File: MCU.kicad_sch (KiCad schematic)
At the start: 35 parts, among them IC9 ATSAMD21G18A-MF, J10 SAMTEC_SSW-106-01-L-S, J7 SAMTEC_SSW-108-01-G-S, J8 SAMTEC_SSW-110-01-G-S, J9 SAMTEC_SSW-108-01-G-S, Q1 XTAL_32.768KHZ_ABRACON_ABS09-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

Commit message: Added new ADC
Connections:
- net MCU_SCL: no longer IC9.32 (PA23), J8.10
- net MCU_SDA: no longer IC9.31 (PA22), J8.9
- net MCU_RxD renamed MCU_RX
- net MCU_TxD renamed MCU_TX
- new net P.A22: IC9.31 (PA22), J8.9
- new net P.A23: IC9.32 (PA23), J8.10
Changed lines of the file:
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@@
 		)
 	)
-	(text_box "Routing note:\n- Placement of female headers must match Arduino Zero Hat"
+	(text_box "Routing note:\n- Placement of female headers must match Arduino Zero Shield"
 		(exclude_from_sim no)
 		(at 285.75 43.18 0)
@@
 		)
 	)
-	(label "MCU_RxD"
+	(label "MCU_RX"
 		(at 201.93 68.58 180)
 		(fields_autoplaced yes)
@@
 		)
 	)
-	(label "MCU_TxD"
+	(label "MCU_TX"
 		(at 350.52 36.83 0)
 		(fields_autoplaced yes)
@@
 		)
 	)
-	(label "P.A22"
+	(label "MCU_SDA"
 		(at 350.52 29.21 0)
 		(fields_autoplaced yes)
@@
 		)
 	)
-	(label "MCU_RxD"
+	(label "MCU_RX"
 		(at 350.52 40.64 0)
 		(fields_autoplaced yes)
@@
 		)
 	)
-	(label "P.A23"
+	(label "MCU_SCL"
 		(at 350.52 33.02 0)
 		(fields_autoplaced yes)
@@
 		)
 	)
-	(label "MCU_TxD"
+	(label "MCU_TX"
 		(at 201.93 66.04 180)
 		(fields_autoplaced yes)
@@
 		)
 	)
-	(label "P.A22"
+	(label "MCU_SDA"
 		(at 107.95 111.76 180)
 		(fields_autoplaced yes)
@@
 		)
 	)
-	(label "P.A23"
+	(label "MCU_SCL"
 		(at 107.95 114.3 180)
 		(fields_autoplaced yes)
@@
 		)
 	)
-	(hierarchical_label "MCU_TxD"
+	(hierarchical_label "MCU_TX"
 		(shape output)
 		(at 374.65 36.83 0)
@@
 		)
 	)
-	(hierarchical_label "MCU_RxD"
+	(hierarchical_label "MCU_RX"
 		(shape input)
 		(at 374.65 40.64 0)

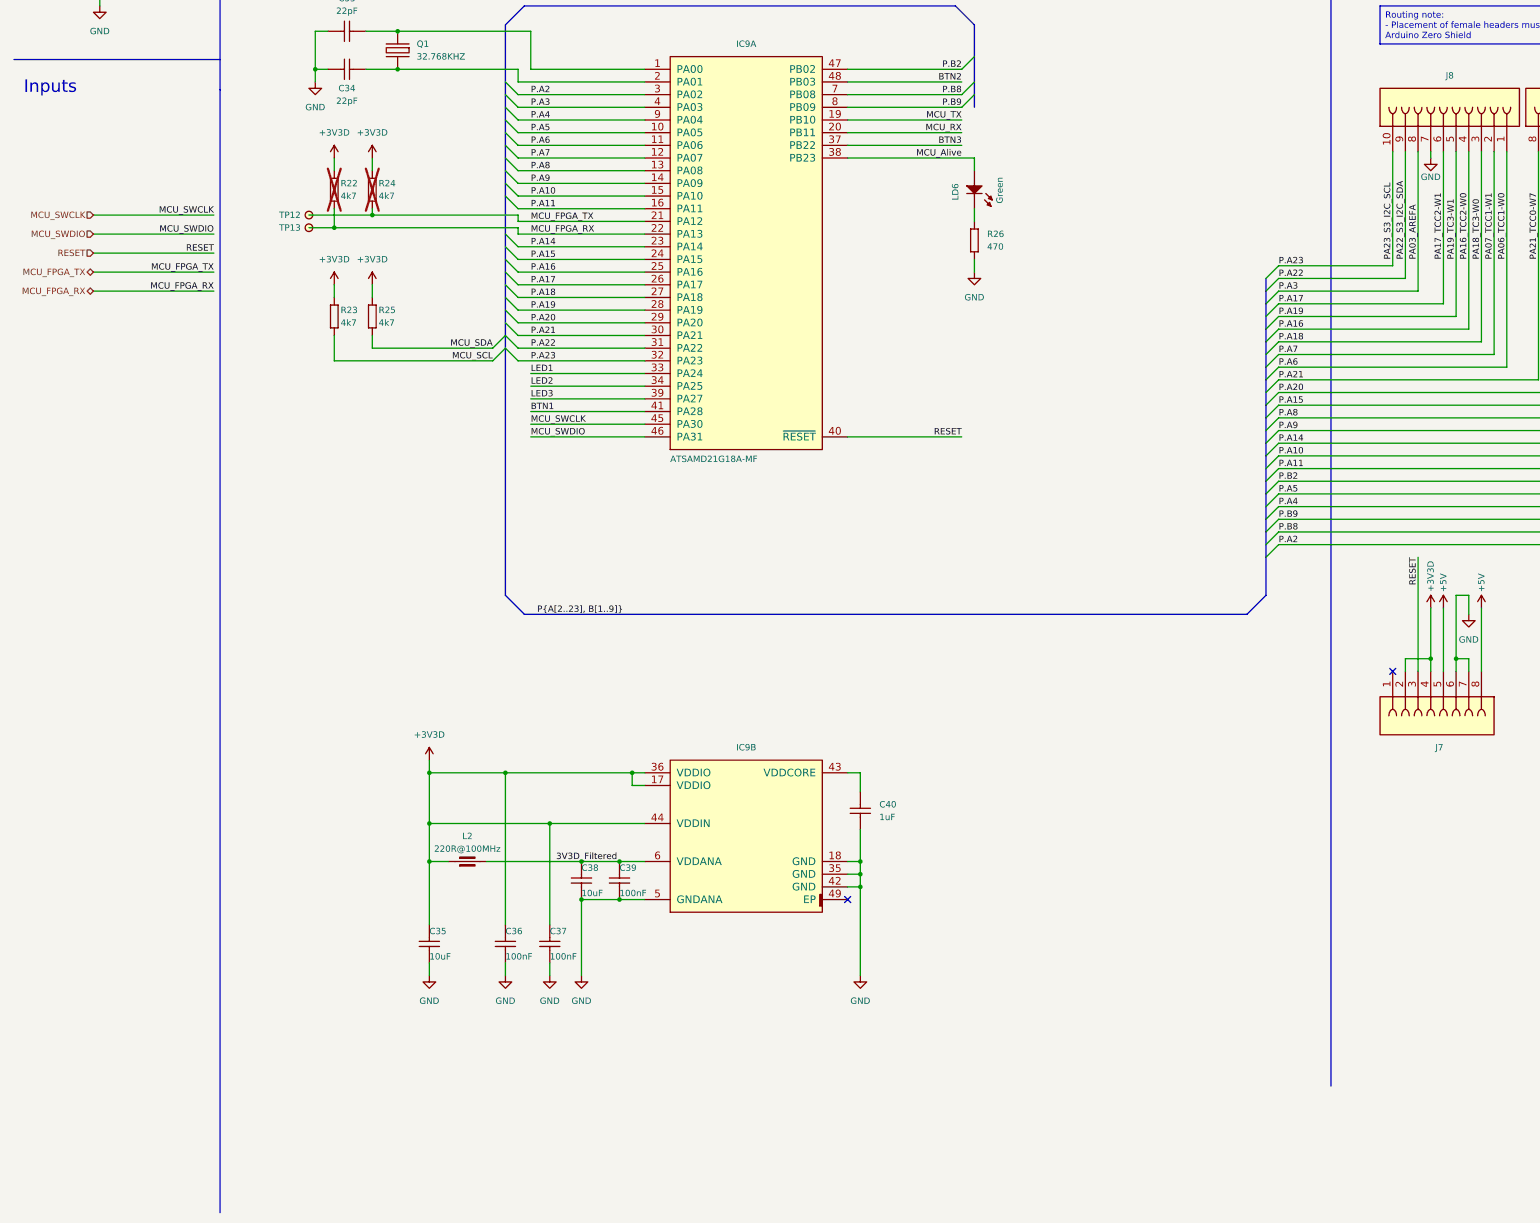
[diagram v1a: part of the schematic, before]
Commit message: Implemented MCU changes (reset mainly) and some cosmetics (USB port)
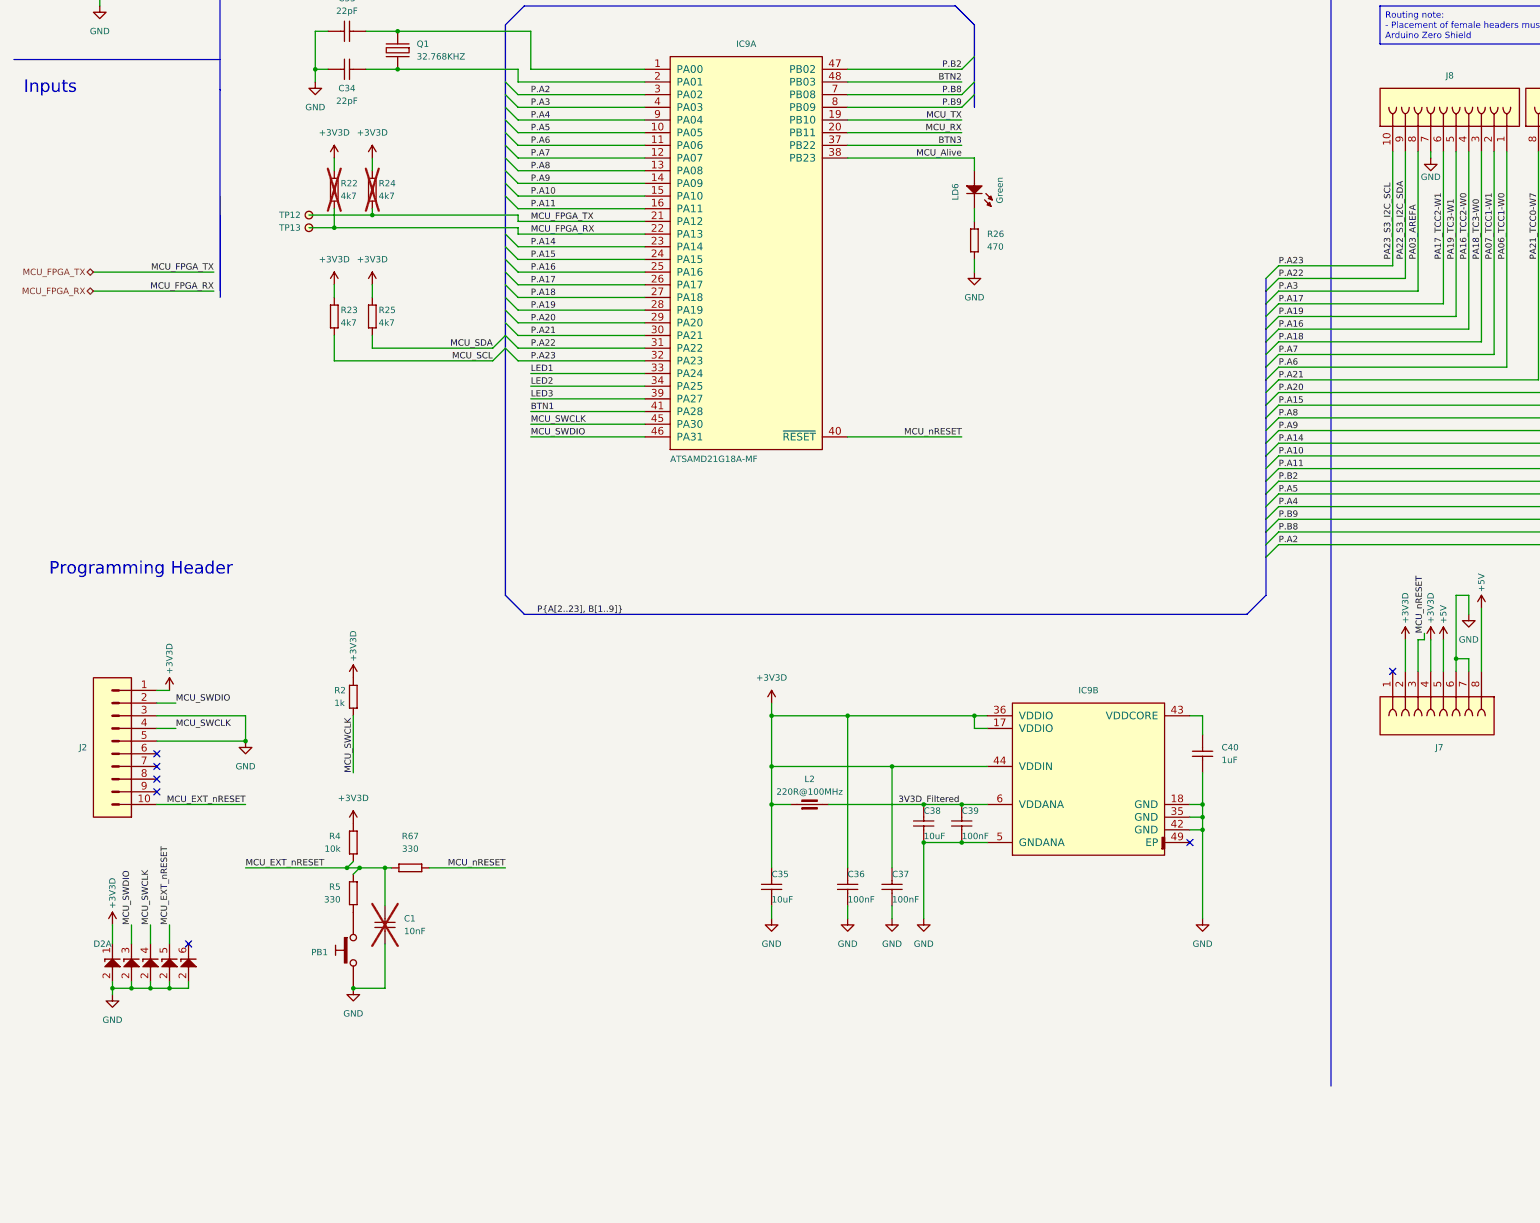
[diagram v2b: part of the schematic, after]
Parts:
- added C1: CC0603_10NF_50V_10%_X7R, Capacitors SMD:CAPC1608X87N, symbol Capacitors SMD:CC0603_10NF_50V_10%_X7R
- added D2: PESD3V3L5UY, ICs And Semiconductors SMD:SOT65P210X110-6N, symbol Diodes:PESD3V3L5UY
- added J2: SAMTEC_FTSH-105-01-L-DV-K, SAMTEC SMD:SAMTEC_FTSH-105-01-L-DV-K, symbol SAMTEC:SAMTEC_FTSH-105-01-L-DV-K
- added PB1: PB_C&K_KSC321JLFS, Switches:PB_C&K_KSC321J, symbol Switches:PB_C&K_KSC321JLFS
- added R2: R0603_1K_1%_0.1W_100PPM, Resistors SMD:RESC1608X55N, symbol Resistors SMD:R0603_1K_1%_0.1W_100PPM
- added R4: R0603_10K_1%_0.1W_100PPM, Resistors SMD:RESC1608X55N, symbol Resistors SMD:R0603_10K_1%_0.1W_100PPM
- added R5, R67: R0603_330R_1%_0.1W_100PPM, Resistors SMD:RESC1608X55N, symbol Resistors SMD:R0603_330R_1%_0.1W_100PPM
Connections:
- net +3V3D: now also D2.1 (C), J2.1, R2.1, R4.1
- net GND: now also C1.2, D2.2 (A), D2.2 (A), D2.2 (A), D2.2 (A), D2.2 (A), J2.3, J2.5, PB1.3, PB1.4
- net MCU_SWCLK: now also D2.4 (C), J2.4, R2.2
- net MCU_SWDIO: now also D2.3 (C), J2.2
- net RESET renamed MCU_nRESET
- net MCU_nRESET: now also R67.2
- new net: PB1.1, PB1.2, R5.2
- new net MCU_EXT_nRESET: C1.1, D2.5 (C), J2.10, R4.2, R5.1, R67.1
- no-connect marks 2 -> 7
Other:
- note added: "Programming Header"
- moved on the sheet: C35, C36, C37, C38, C39, C40, IC9B, L2

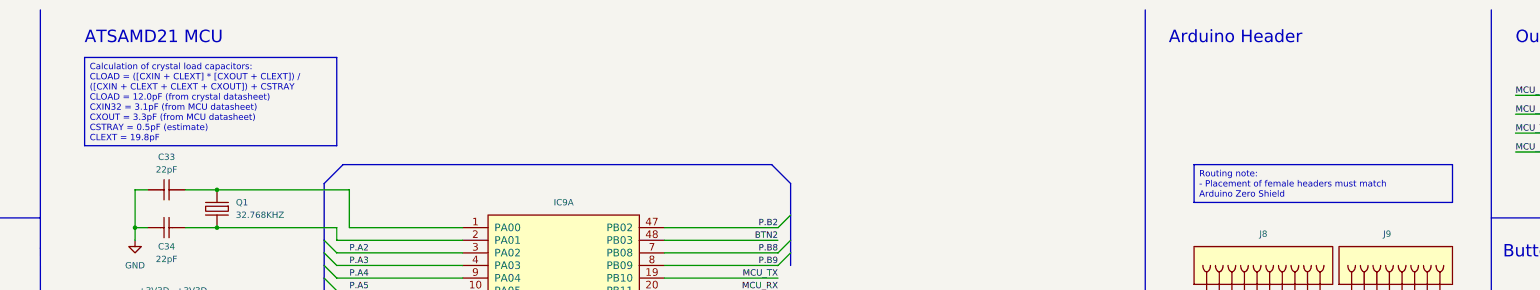
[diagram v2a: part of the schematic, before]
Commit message: Rename Power Supply sheet, remove iCE programming option
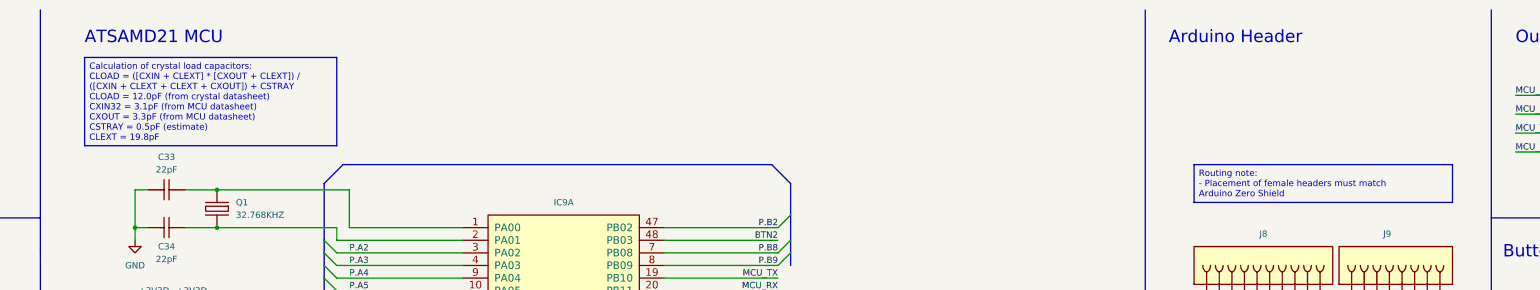
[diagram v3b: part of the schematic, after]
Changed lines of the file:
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@@
 (kicad_sch
-	(version 20231120)
+	(version 20240812)
 	(generator "eeschema")
-	(generator_version "8.0")
+	(generator_version "8.99")
 	(paper "A3")
 	(title_block
@@
 		(comment 7 "2023-10-06")
 	)
+	(text "Buttons"
+		(exclude_from_sim no)
+		(at 347.98 62.23 0)
+		(effects
+			(font
+				(size 2.5 2.5)
+			)
+			(justify left bottom)
+		)
+	)
+	(text "Programming Header"
+		(exclude_from_sim no)
+		(at 19.05 157.48 0)
+		(effects
+			(font
+				(size 2.5 2.5)
+			)
+			(justify left bottom)
+		)
+	)
+	(text "ATSAMD21 MCU"
+		(exclude_from_sim no)
+		(at 62.23 19.05 0)
+		(effects
+			(font
+				(size 2.5 2.5)
+			)
+			(justify left bottom)
+		)
+	)
+	(text "LEDs"
+		(exclude_from_sim no)
+		(at 349.25 152.4 0)
+		(effects
+			(font
+				(size 2.5 2.5)
+			)
+			(justify left bottom)
+		)
+	)
+	(text "Inputs"
+		(exclude_from_sim no)
+		(at 13.97 60.96 0)
+		(effects
+			(font
+				(size 2.5 2.5)
+			)
+			(justify left bottom)
+		)
+	)
+	(text "Outputs"
+		(exclude_from_sim no)
+		(at 350.52 19.05 0)
+		(effects
+			(font
+				(size 2.5 2.5)
+			)
+			(justify left bottom)
+		)
+	)
+	(text "Power Ports"
+		(exclude_from_sim no)
+		(at 15.24 19.05 0)
+		(effects
+			(font
+				(size 2.5 2.5)
+			)
+			(justify left bottom)
+		)
+	)
+	(text "Arduino Header"
+		(exclude_from_sim no)
+		(at 280.67 19.05 0)
+		(effects
+			(font
+				(size 2.5 2.5)
+			)
+			(justify left bottom)
+		)
+	)
+	(text_box "Calculation of crystal load capacitors:\nCLOAD = ([CXIN + CLEXT] * [CXOUT + CLEXT]) / ([CXIN + CLEXT + CLEXT + CXOUT]) + CSTRAY\nCLOAD = 12.0pF (from crystal datasheet)\nCXIN32 = 3.1pF (from MCU datasheet)\nCXOUT = 3.3pF (from MCU datasheet)\nCSTRAY = 0.5pF (estimate)\nCLEXT = 19.8pF"
+		(exclude_from_sim no)
+		(at 62.23 21.59 0)
+		(size 50.8 17.78)
+		(margins 0.9525 0.9525 0.9525 0.9525)
+		(stroke
+			(width 0)
+			(type default)
+		)
+		(fill
+			(type none)
+		)
+		(effects
+			(font
+				(size 1.27 1.27)
+			)
+			(justify left top)
+		)
+	)
+	(text_box "Routing note:\n- Placement of female headers must match Arduino Zero Shield"
+		(exclude_from_sim no)
+		(at 285.75 43.18 0)
+		(size 52.07 7.62)
+		(margins 0.9525 0.9525 0.9525 0.9525)
+		(stroke
+			(width 0)
+			(type default)
+			(color 255 109 0 1)
+		)
+		(fill
+			(type none)
+		)
+		(effects
+			(font
+				(size 1.27 1.27)
+				(color 255 109 0 1)
+			)
+			(justify left top)
+		)
+	)
 	(junction
 		(at 35.56 240.03)
@@
 		)
 	)
-	(text_box "Calculation of crystal load capacitors:\nCLOAD = ([CXIN + CLEXT] * [CXOUT + CLEXT]) / ([CXIN + CLEXT + CLEXT + CXOUT]) + CSTRAY\nCLOAD = 12.0pF (from crystal datasheet)\nCXIN32 = 3.1pF (from MCU datasheet)\nCXOUT = 3.3pF (from MCU datasheet)\nCSTRAY = 0.5pF (estimate)\nCLEXT = 19.8pF"
-		(exclude_from_sim no)
-		(at 62.23 21.59 0)
-		(size 50.8 17.78)
-		(stroke
-			(width 0)
-			(type default)
-		)
-		(fill
-			(type none)
-		)
-		(effects
-			(font
-				(size 1.27 1.27)
-			)
-			(justify left top)
-		)
-	)
-	(text_box "Routing note:\n- Placement of female headers must match Arduino Zero Shield"
-		(exclude_from_sim no)
-		(at 285.75 43.18 0)
-		(size 52.07 7.62)
-		(stroke
-			(width 0)
-			(type default)
-			(color 255 109 0 1)
-		)
-		(fill
-			(type none)
-		)
-		(effects
-			(font
-				(size 1.27 1.27)
-				(color 255 109 0 1)
-			)
-			(justify left top)
-		)
-	)
-	(text "Buttons"
-		(exclude_from_sim no)
-		(at 347.98 62.23 0)
-		(effects
-			(font
-				(size 2.5 2.5)
-			)
-			(justify left bottom)
-		)
-	)
-	(text "Programming Header"
-		(exclude_from_sim no)
-		(at 19.05 157.48 0)
-		(effects
-			(font
-				(size 2.5 2.5)
-			)
-			(justify left bottom)
-		)
-	)
-	(text "ATSAMD21 MCU"
-		(exclude_from_sim no)
-		(at 62.23 19.05 0)
-		(effects
-			(font
-				(size 2.5 2.5)
-			)
-			(justify left bottom)
-		)
-	)
-	(text "LEDs"
-		(exclude_from_sim no)
-		(at 349.25 152.4 0)
-		(effects
-			(font
-				(size 2.5 2.5)
-			)
-			(justify left bottom)
-		)
-	)
-	(text "Inputs"
-		(exclude_from_sim no)
-		(at 13.97 60.96 0)
-		(effects
-			(font
-				(size 2.5 2.5)
-			)
-			(justify left bottom)
-		)
-	)
-	(text "Outputs"
-		(exclude_from_sim no)
-		(at 350.52 19.05 0)
-		(effects
-			(font
-				(size 2.5 2.5)
-			)
-			(justify left bottom)
-		)
-	)
-	(text "Power Ports"
-		(exclude_from_sim no)
-		(at 15.24 19.05 0)
-		(effects
-			(font
-				(size 2.5 2.5)
-			)
-			(justify left bottom)
-		)
-	)
-	(text "Arduino Header"
-		(exclude_from_sim no)
-		(at 280.67 19.05 0)
-		(effects
-			(font
-				(size 2.5 2.5)
-			)
-			(justify left bottom)
-		)
-	)

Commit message: Rename FPGA_PROG bus for mor clarity + small changes
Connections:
- net MCU_nRESET renamed DTR
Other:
- note added: "TO CHECK:"
- moved on the sheet: C1, PB1, PB2, PB3, PB4, R29, R30, R34, R4, R5, R67

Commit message: REV2 modifications completed
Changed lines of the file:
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@@
 		(comment 1 "CROME")
 		(comment 3 "RP-IL")
-		(comment 6 "Håkon Liverud")
+		(comment 6 "Liverud, Consani")
 		(comment 7 "2023-10-06")
 	)
@@
 		)
 	)
-	(text_box "Routing note:\nplace BTN1 (PB4) rightmost, then BTN2 and BTN3 leftmost\n"
+	(text_box "Routing note:\n- REV2: Place BTN1 (PB4) rightmost, then BTN2 and BTN3 leftmost\n"
 		(exclude_from_sim no)
 		(at 360.68 124.46 0)

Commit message: REV2 feedback modifications
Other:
- note added: "MCU Reset:"
- note removed: "TO CHECK:"
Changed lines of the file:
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@@
 	(title_block
 		(title "ACCURATE 2 Evaluation Board")
-		(date "2023-10-06")
+		(date "2025-01-22")
 		(rev "A")
 		(company "CERN")
@@
 		(comment 3 "RP-IL")
 		(comment 6 "Liverud, Consani")
-		(comment 7 "2023-10-06")
 	)
 	(text "Buttons"
@@
 		)
 	)
-	(text "TO CHECK:"
+	(text "MCU Reset:"
 		(exclude_from_sim no)
 		(at 82.55 218.44 0)
